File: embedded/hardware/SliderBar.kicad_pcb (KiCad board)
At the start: 2 copper layers, 101.6 x 25.4 mm, 35 parts, among them J1 USB_B_Mini, J2 MOTOR_OUT, J3 POT_IN, J4 DEBUG, U1 MIC5205-3.3YM5, U2 TB6612FNG, U3 MT3608, U4 STM32F072C8Tx

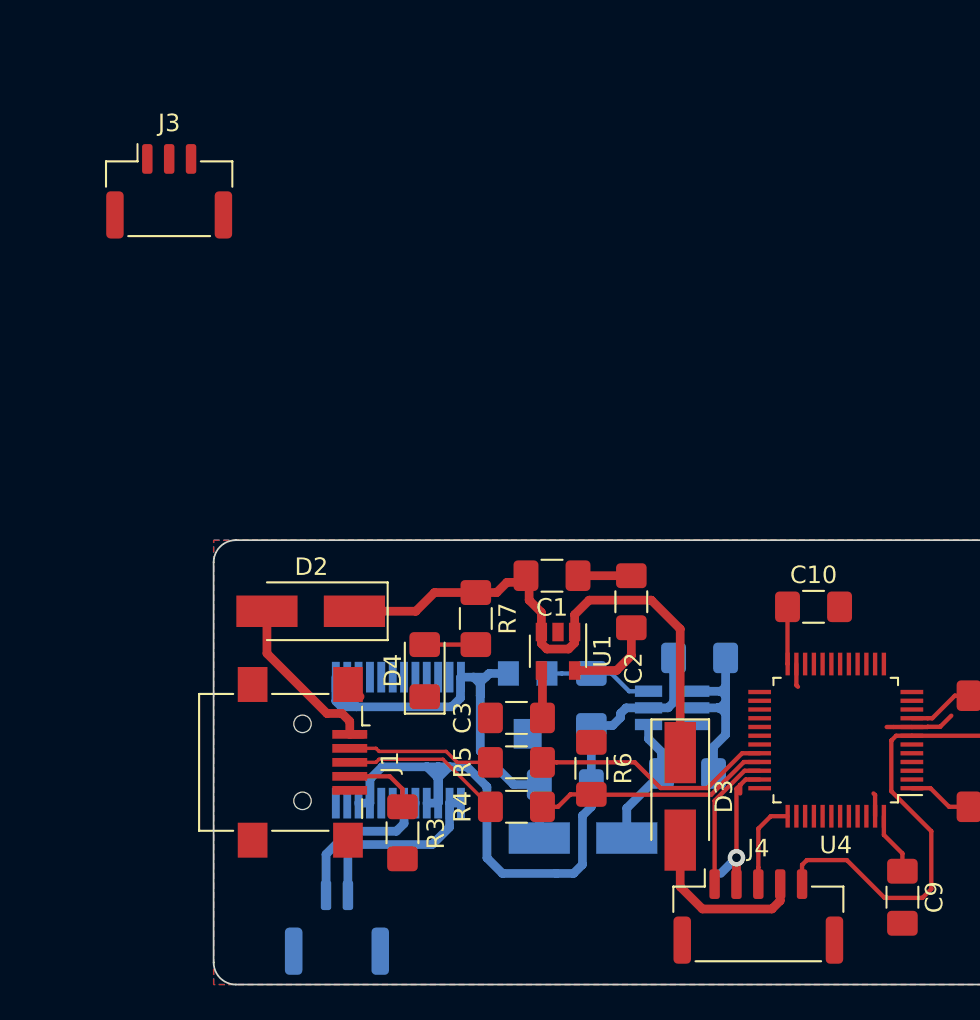
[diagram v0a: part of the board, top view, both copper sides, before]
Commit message: Change connector footprints to JST GH 1.25mm
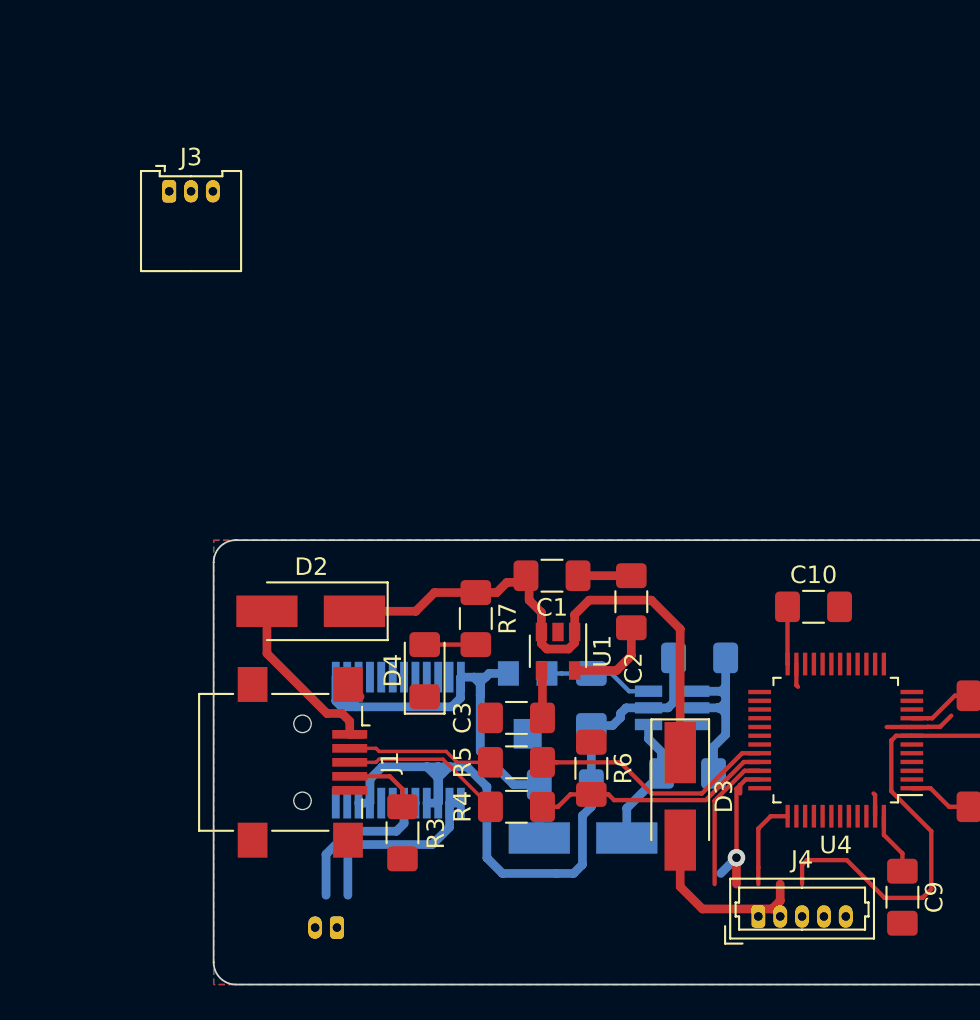
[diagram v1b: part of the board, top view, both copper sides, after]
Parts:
- J2: footprint Connector_JST:JST_GH_SM02B-GHS-TB_1x02-1MP_P1.25mm_Horizontal -> Connector_Molex:Molex_PicoBlade_53048-0210_1x02_P1.25mm_Horizontal
- J3: footprint Connector_JST:JST_GH_SM03B-GHS-TB_1x03-1MP_P1.25mm_Horizontal -> Connector_Molex:Molex_PicoBlade_53048-0310_1x03_P1.25mm_Horizontal
- J4: footprint Connector_JST:JST_GH_SM05B-GHS-TB_1x05-1MP_P1.25mm_Horizontal -> Connector_Molex:Molex_PicoBlade_53047-0510_1x05_P1.25mm_Vertical

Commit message: Add HTML bom
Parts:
- C13, C14, R8: moved to B.Cu
- moved R8 87.3 mm to (127.9, 102.4), turned to 180 degrees
- moved C14 71.3 mm to (98.4, 93.3), turned to 270 degrees
- moved C13 71.0 mm to (110.1, 87.6)
- moved J3 61.0 mm to (139.1, 103.5)
- moved C11 43.2 mm to (68.5, 87.1)
- moved C12 17.0 mm to (74.9, 102.9)
- moved J2 1.91 mm to (102.9, 104.1)
- moved J4 1.47 mm to (125.1, 106.0)
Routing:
- net STBY: track 0.00 -> 35.8 mm, vias 0 -> 1
- net GND: track 61.1 -> 75.2 mm, vias 1 -> 0
- net +10V: track 28.7 -> 35.7 mm
- net Net-(R8-Pad1): track 0.00 -> 4.96 mm, vias 0 -> 1
- net VPP: track 10.1 -> 13.4 mm
- net SWDIO: track 8.05 -> 11.2 mm
- net NRST: track 28.5 -> 26.1 mm
- net SWCLK: track 5.14 -> 6.64 mm
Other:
- board size 101.6 x 25.4 mm -> 54.7 x 25.4 mm

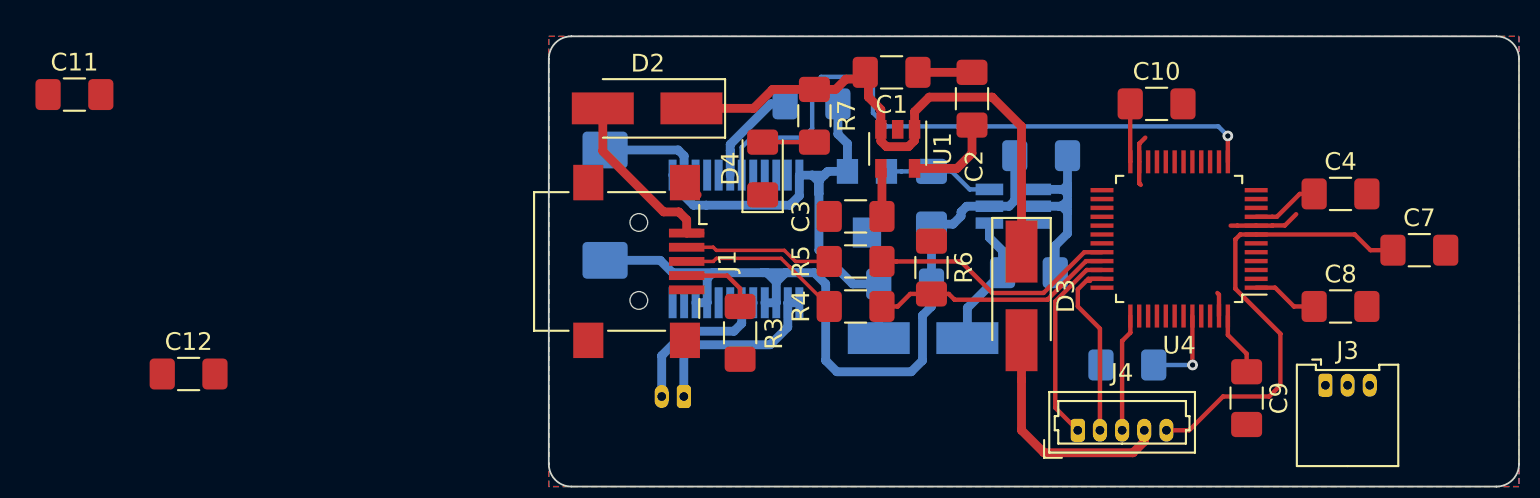
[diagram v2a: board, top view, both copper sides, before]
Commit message: Fix lot of footprints, Add mounting holes
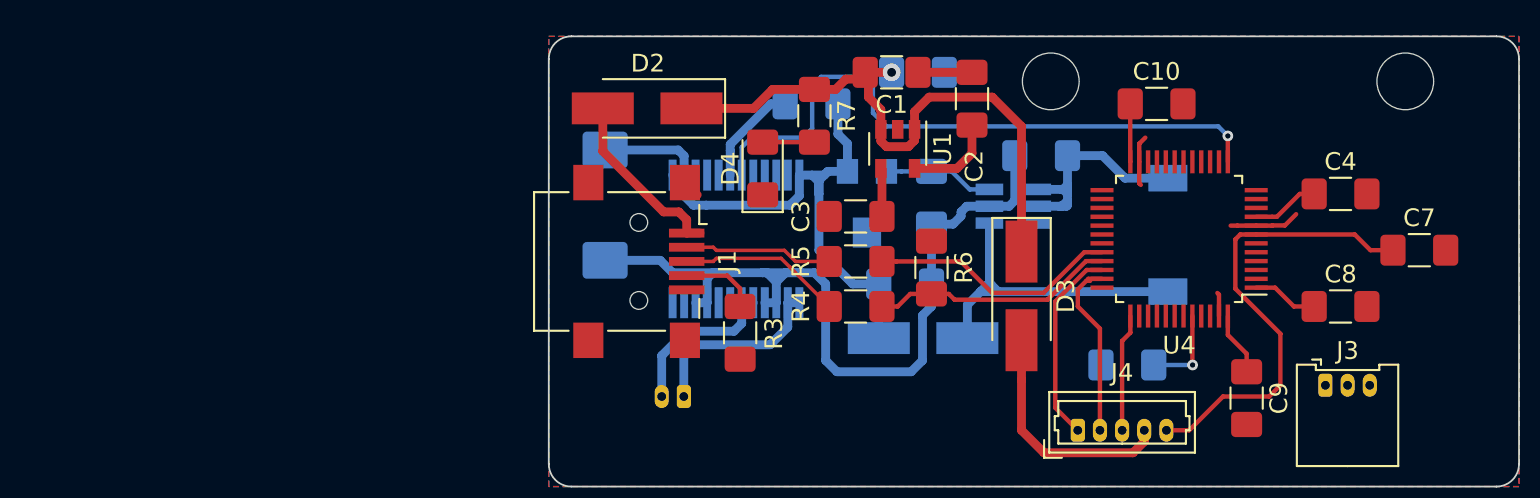
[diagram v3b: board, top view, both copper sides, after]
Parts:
- removed C12: 470µ, Capacitor_SMD:C_1206_3216Metric_Pad1.42x1.75mm_HandSolder
- added H1: MountingHole, MountingHole:MountingHole_3.2mm_M3_ISO14580, F.Cu at (123.6, 86.4)
- added H2: MountingHole, MountingHole:MountingHole_3.2mm_M3_ISO14580, F.Cu at (143.6, 86.4)
- C11: moved to B.Cu
- L1: footprint Inductor_SMD:L_1206_3216Metric_Pad1.42x1.75mm_HandSolder -> Inductor_SMD:L_7.3x7.3_H3.5
- moved C11 47.6 mm to (116.1, 85.9)
- moved L1 8.12 mm to (130.2, 95.0), turned to 90 degrees
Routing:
- net Net-(D1-Pad2): track 8.01 -> 18.7 mm
- net +5V: track 45.0 -> 48.2 mm, vias 0 -> 1
